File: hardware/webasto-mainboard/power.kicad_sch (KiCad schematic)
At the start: 14 parts, among them U5 BD9G341EFJ

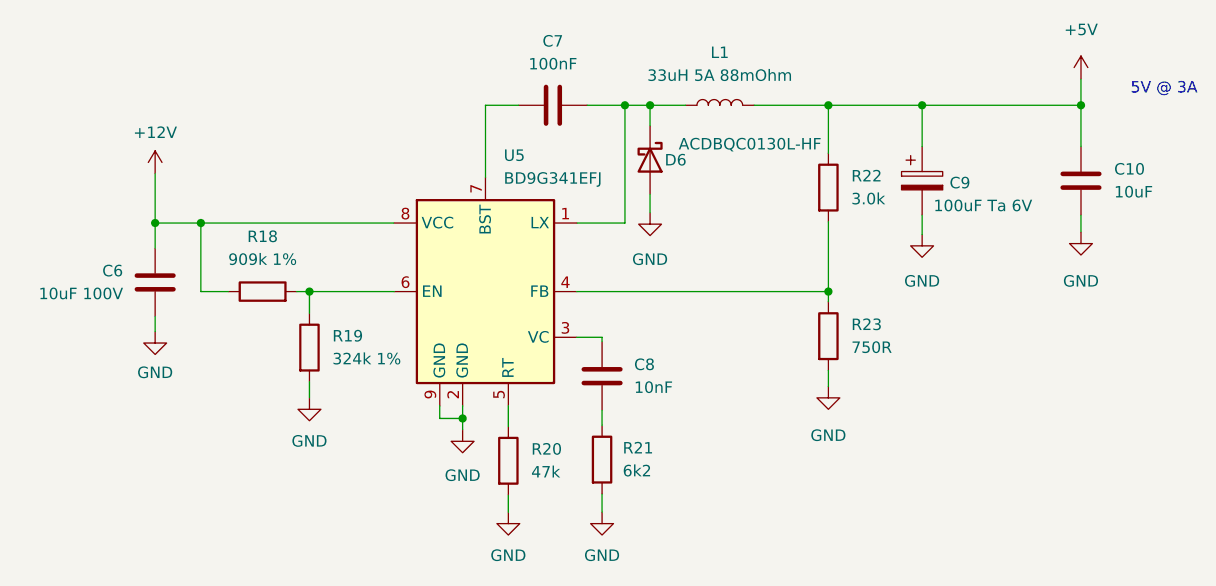
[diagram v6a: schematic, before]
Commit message: Oops.  StartRun is active at +12V.  Change the level translation.
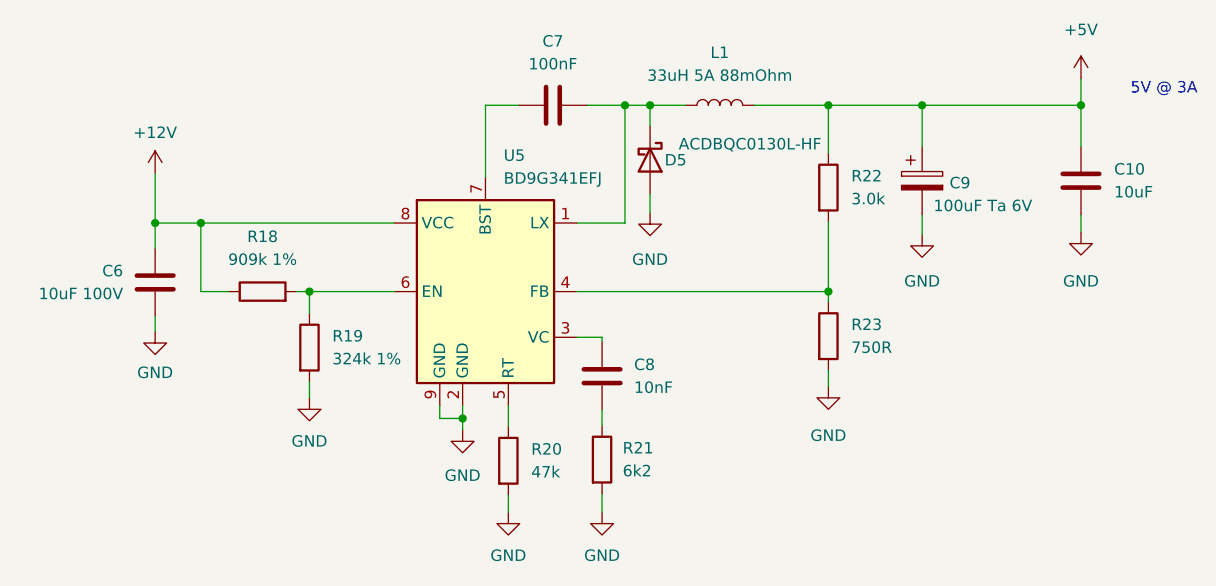
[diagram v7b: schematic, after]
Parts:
- renumbered D6 to D5
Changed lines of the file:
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@@
   (symbol (lib_id "Device:D_Schottky") (at 163.068 65.278 270) (unit 1)
     (in_bom yes) (on_board yes)
-    (property "Reference" "D6" (id 0) (at 167.132 65.278 90)
+    (property "Reference" "D5" (id 0) (at 167.132 65.278 90)
       (effects (font (size 1.27 1.27)) (justify right))
     )
@@
   (symbol (lib_id "power:GND") (at 210.947 73.279 0) (unit 1)
     (in_bom yes) (on_board yes) (fields_autoplaced)
-    (property "Reference" "#PWR052" (id 0) (at 210.947 79.629 0)
+    (property "Reference" "#PWR053" (id 0) (at 210.947 79.629 0)
       (effects (font (size 1.27 1.27)) hide)
     )
@@
   (symbol (lib_id "power:GND") (at 163.068 71.12 0) (unit 1)
     (in_bom yes) (on_board yes) (fields_autoplaced)
-    (property "Reference" "#PWR048" (id 0) (at 163.068 77.47 0)
+    (property "Reference" "#PWR049" (id 0) (at 163.068 77.47 0)
       (effects (font (size 1.27 1.27)) hide)
     )
@@
   (symbol (lib_id "power:GND") (at 193.294 73.533 0) (unit 1)
     (in_bom yes) (on_board yes) (fields_autoplaced)
-    (property "Reference" "#PWR050" (id 0) (at 193.294 79.883 0)
+    (property "Reference" "#PWR051" (id 0) (at 193.294 79.883 0)
       (effects (font (size 1.27 1.27)) hide)
     )
@@
   (symbol (lib_id "power:GND") (at 108.077 84.328 0) (unit 1)
     (in_bom yes) (on_board yes) (fields_autoplaced)
-    (property "Reference" "#PWR043" (id 0) (at 108.077 90.678 0)
+    (property "Reference" "#PWR044" (id 0) (at 108.077 90.678 0)
       (effects (font (size 1.27 1.27)) hide)
     )
@@
   (symbol (lib_id "power:GND") (at 142.24 95.25 0) (unit 1)
     (in_bom yes) (on_board yes) (fields_autoplaced)
-    (property "Reference" "#PWR045" (id 0) (at 142.24 101.6 0)
+    (property "Reference" "#PWR046" (id 0) (at 142.24 101.6 0)
       (effects (font (size 1.27 1.27)) hide)
     )
@@
   (symbol (lib_id "power:GND") (at 125.222 91.694 0) (unit 1)
     (in_bom yes) (on_board yes) (fields_autoplaced)
-    (property "Reference" "#PWR044" (id 0) (at 125.222 98.044 0)
+    (property "Reference" "#PWR045" (id 0) (at 125.222 98.044 0)
       (effects (font (size 1.27 1.27)) hide)
     )
@@
   (symbol (lib_id "power:+12V") (at 108.077 66.802 0) (unit 1)
     (in_bom yes) (on_board yes) (fields_autoplaced)
-    (property "Reference" "#PWR042" (id 0) (at 108.077 70.612 0)
+    (property "Reference" "#PWR043" (id 0) (at 108.077 70.612 0)
       (effects (font (size 1.27 1.27)) hide)
     )
@@
   (symbol (lib_id "power:GND") (at 182.88 90.424 0) (unit 1)
     (in_bom yes) (on_board yes) (fields_autoplaced)
-    (property "Reference" "#PWR049" (id 0) (at 182.88 96.774 0)
+    (property "Reference" "#PWR050" (id 0) (at 182.88 96.774 0)
       (effects (font (size 1.27 1.27)) hide)
     )
@@
   (symbol (lib_id "power:+5V") (at 210.947 56.261 0) (unit 1)
     (in_bom yes) (on_board yes) (fields_autoplaced)
-    (property "Reference" "#PWR051" (id 0) (at 210.947 60.071 0)
+    (property "Reference" "#PWR052" (id 0) (at 210.947 60.071 0)
       (effects (font (size 1.27 1.27)) hide)
     )
@@
   (symbol (lib_id "power:GND") (at 147.32 104.394 0) (unit 1)
     (in_bom yes) (on_board yes) (fields_autoplaced)
-    (property "Reference" "#PWR046" (id 0) (at 147.32 110.744 0)
+    (property "Reference" "#PWR047" (id 0) (at 147.32 110.744 0)
       (effects (font (size 1.27 1.27)) hide)
     )
@@
   (symbol (lib_id "power:GND") (at 157.734 104.394 0) (unit 1)
     (in_bom yes) (on_board yes) (fields_autoplaced)
-    (property "Reference" "#PWR047" (id 0) (at 157.734 110.744 0)
-      (effects (font (size 1.27 1.27)) hide)
-    )
+    (property "Reference" "#PWR048" (id 0) (at 157.734 110.744 0)
+      (effects (font (size 1.27 1.27)) hide)
+    )

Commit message: Added the LEDs onto the board and init
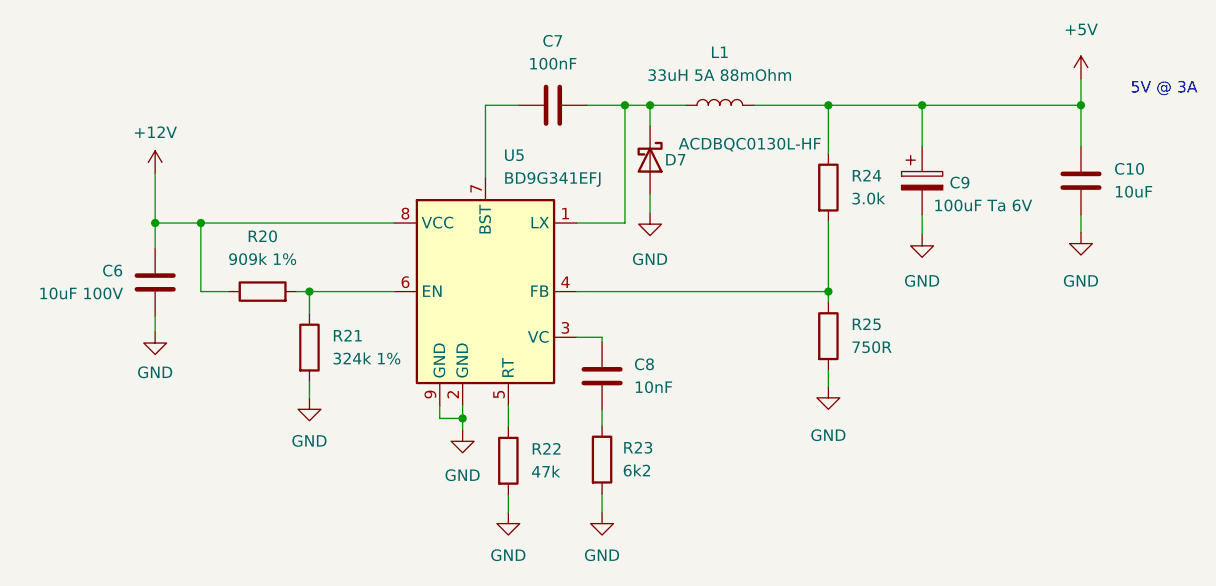
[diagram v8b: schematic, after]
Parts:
- renumbered D5 to D7, R18 to R20, R19 to R21, R20 to R22, R21 to R23, R22 to R24, R23 to R25
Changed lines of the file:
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@@
   (symbol (lib_id "Device:D_Schottky") (at 163.068 65.278 270) (unit 1)
     (in_bom yes) (on_board yes)
-    (property "Reference" "D5" (id 0) (at 167.132 65.278 90)
+    (property "Reference" "D7" (id 0) (at 167.132 65.278 90)
       (effects (font (size 1.27 1.27)) (justify right))
     )
@@
   (symbol (lib_id "Device:R") (at 125.222 86.106 0) (unit 1)
     (in_bom yes) (on_board yes) (fields_autoplaced)
-    (property "Reference" "R19" (id 0) (at 127.762 84.8359 0)
+    (property "Reference" "R21" (id 0) (at 127.762 84.8359 0)
       (effects (font (size 1.27 1.27)) (justify left))
     )
@@
   (symbol (lib_id "power:GND") (at 210.947 73.279 0) (unit 1)
     (in_bom yes) (on_board yes) (fields_autoplaced)
-    (property "Reference" "#PWR053" (id 0) (at 210.947 79.629 0)
+    (property "Reference" "#PWR055" (id 0) (at 210.947 79.629 0)
       (effects (font (size 1.27 1.27)) hide)
     )
@@
   (symbol (lib_id "Device:R") (at 147.32 98.679 0) (unit 1)
     (in_bom yes) (on_board yes) (fields_autoplaced)
-    (property "Reference" "R20" (id 0) (at 149.86 97.4089 0)
+    (property "Reference" "R22" (id 0) (at 149.86 97.4089 0)
       (effects (font (size 1.27 1.27)) (justify left))
     )
@@
   (symbol (lib_id "power:GND") (at 163.068 71.12 0) (unit 1)
     (in_bom yes) (on_board yes) (fields_autoplaced)
-    (property "Reference" "#PWR049" (id 0) (at 163.068 77.47 0)
+    (property "Reference" "#PWR051" (id 0) (at 163.068 77.47 0)
       (effects (font (size 1.27 1.27)) hide)
     )
@@
   (symbol (lib_id "Device:R") (at 182.88 68.326 0) (unit 1)
     (in_bom yes) (on_board yes) (fields_autoplaced)
-    (property "Reference" "R22" (id 0) (at 185.42 67.0559 0)
+    (property "Reference" "R24" (id 0) (at 185.42 67.0559 0)
       (effects (font (size 1.27 1.27)) (justify left))
     )
@@
   (symbol (lib_id "power:GND") (at 193.294 73.533 0) (unit 1)
     (in_bom yes) (on_board yes) (fields_autoplaced)
-    (property "Reference" "#PWR051" (id 0) (at 193.294 79.883 0)
+    (property "Reference" "#PWR053" (id 0) (at 193.294 79.883 0)
       (effects (font (size 1.27 1.27)) hide)
     )
@@
   (symbol (lib_id "Device:R") (at 182.88 84.836 0) (unit 1)
     (in_bom yes) (on_board yes) (fields_autoplaced)
-    (property "Reference" "R23" (id 0) (at 185.42 83.5659 0)
+    (property "Reference" "R25" (id 0) (at 185.42 83.5659 0)
       (effects (font (size 1.27 1.27)) (justify left))
     )
@@
   (symbol (lib_id "power:GND") (at 108.077 84.328 0) (unit 1)
     (in_bom yes) (on_board yes) (fields_autoplaced)
-    (property "Reference" "#PWR044" (id 0) (at 108.077 90.678 0)
+    (property "Reference" "#PWR046" (id 0) (at 108.077 90.678 0)
       (effects (font (size 1.27 1.27)) hide)
     )
@@
   (symbol (lib_id "power:GND") (at 142.24 95.25 0) (unit 1)
     (in_bom yes) (on_board yes) (fields_autoplaced)
-    (property "Reference" "#PWR046" (id 0) (at 142.24 101.6 0)
+    (property "Reference" "#PWR048" (id 0) (at 142.24 101.6 0)
       (effects (font (size 1.27 1.27)) hide)
     )
@@
   (symbol (lib_id "power:GND") (at 125.222 91.694 0) (unit 1)
     (in_bom yes) (on_board yes) (fields_autoplaced)
-    (property "Reference" "#PWR045" (id 0) (at 125.222 98.044 0)
+    (property "Reference" "#PWR047" (id 0) (at 125.222 98.044 0)
       (effects (font (size 1.27 1.27)) hide)
     )
@@
   (symbol (lib_id "power:+12V") (at 108.077 66.802 0) (unit 1)
     (in_bom yes) (on_board yes) (fields_autoplaced)
-    (property "Reference" "#PWR043" (id 0) (at 108.077 70.612 0)
+    (property "Reference" "#PWR045" (id 0) (at 108.077 70.612 0)
       (effects (font (size 1.27 1.27)) hide)
     )
@@
   (symbol (lib_id "power:GND") (at 182.88 90.424 0) (unit 1)
     (in_bom yes) (on_board yes) (fields_autoplaced)
-    (property "Reference" "#PWR050" (id 0) (at 182.88 96.774 0)
+    (property "Reference" "#PWR052" (id 0) (at 182.88 96.774 0)
       (effects (font (size 1.27 1.27)) hide)
     )
@@
   (symbol (lib_id "power:+5V") (at 210.947 56.261 0) (unit 1)
     (in_bom yes) (on_board yes) (fields_autoplaced)
-    (property "Reference" "#PWR052" (id 0) (at 210.947 60.071 0)
+    (property "Reference" "#PWR054" (id 0) (at 210.947 60.071 0)
       (effects (font (size 1.27 1.27)) hide)
     )
@@
   (symbol (lib_id "Device:R") (at 120.015 79.883 90) (unit 1)
     (in_bom yes) (on_board yes) (fields_autoplaced)
-    (property "Reference" "R18" (id 0) (at 120.015 73.787 90))
+    (property "Reference" "R20" (id 0) (at 120.015 73.787 90))
     (property "Value" "909k 1%" (id 1) (at 120.015 76.327 90))
     (property "Footprint" "Resistor_SMD:R_0805_2012Metric_Pad1.20x1.40mm_HandSolder" (id 2) (at 120.015 81.661 90)
@@
   (symbol (lib_id "power:GND") (at 147.32 104.394 0) (unit 1)
     (in_bom yes) (on_board yes) (fields_autoplaced)
-    (property "Reference" "#PWR047" (id 0) (at 147.32 110.744 0)
+    (property "Reference" "#PWR049" (id 0) (at 147.32 110.744 0)
       (effects (font (size 1.27 1.27)) hide)
     )
@@
   (symbol (lib_id "Device:R") (at 157.734 98.552 0) (unit 1)
     (in_bom yes) (on_board yes) (fields_autoplaced)
-    (property "Reference" "R21" (id 0) (at 160.02 97.2819 0)
+    (property "Reference" "R23" (id 0) (at 160.02 97.2819 0)
       (effects (font (size 1.27 1.27)) (justify left))
     )
@@
   (symbol (lib_id "power:GND") (at 157.734 104.394 0) (unit 1)
     (in_bom yes) (on_board yes) (fields_autoplaced)
-    (property "Reference" "#PWR048" (id 0) (at 157.734 110.744 0)
-      (effects (font (size 1.27 1.27)) hide)
-    )
+    (property "Reference" "#PWR050" (id 0) (at 157.734 110.744 0)
+      (effects (font (size 1.27 1.27)) hide)
+    )
